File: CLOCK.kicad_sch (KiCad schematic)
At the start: 5 parts, among them X1 S3D50.000000B20F30T

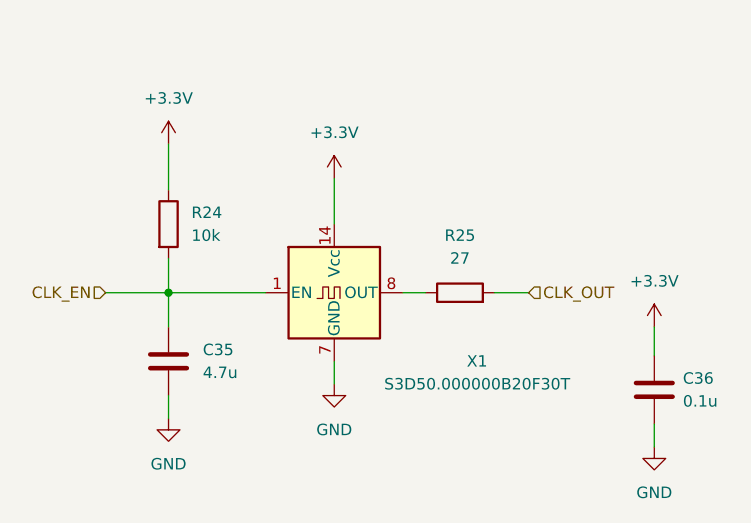
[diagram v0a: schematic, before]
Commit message: Add some more footprints
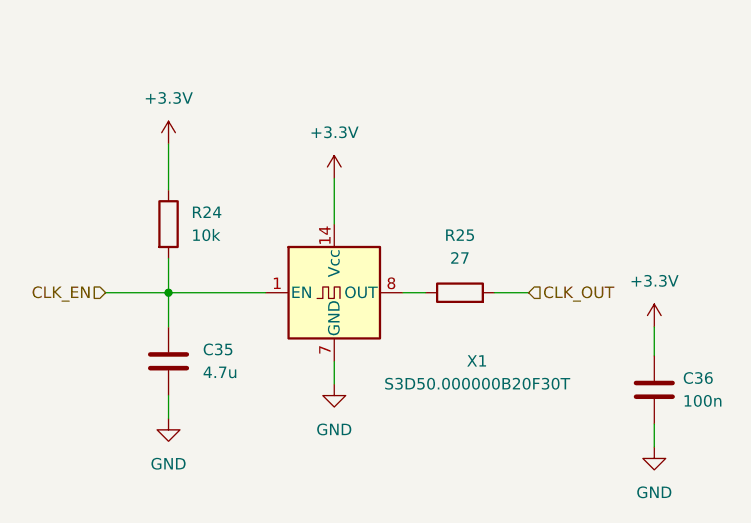
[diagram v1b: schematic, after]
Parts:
- C35: footprint (none) -> Capacitor_SMD:C_0603_1608Metric_Pad1.08x0.95mm_HandSolder
- C36: value 0.1u -> 100n; footprint (none) -> Capacitor_SMD:C_0603_1608Metric_Pad1.08x0.95mm_HandSolder
- R24, R25: footprint (none) -> Resistor_SMD:R_0603_1608Metric_Pad0.98x0.95mm_HandSolder
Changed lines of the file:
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@@
       (effects (font (size 1.27 1.27)) (justify left))
     )
-    (property "Value" "0.1u" (id 1) (at 191.77 108.5849 0)
+    (property "Value" "100n" (id 1) (at 191.77 108.5849 0)
       (effects (font (size 1.27 1.27)) (justify left))
     )
-    (property "Footprint" "" (id 2) (at 189.5602 111.125 0)
+    (property "Footprint" "Capacitor_SMD:C_0603_1608Metric_Pad1.08x0.95mm_HandSolder" (id 2) (at 189.5602 111.125 0)
       (effects (font (size 1.27 1.27)) hide)
     )
@@
       (effects (font (size 1.27 1.27)) (justify left))
     )
-    (property "Footprint" "" (id 2) (at 132.842 88.9 90)
+    (property "Footprint" "Resistor_SMD:R_0603_1608Metric_Pad0.98x0.95mm_HandSolder" (id 2) (at 132.842 88.9 90)
       (effects (font (size 1.27 1.27)) hide)
     )
@@
     (property "Reference" "R25" (id 0) (at 167.005 90.17 90))
     (property "Value" "27" (id 1) (at 167.005 92.71 90))
-    (property "Footprint" "" (id 2) (at 167.005 98.298 90)
+    (property "Footprint" "Resistor_SMD:R_0603_1608Metric_Pad0.98x0.95mm_HandSolder" (id 2) (at 167.005 98.298 90)
       (effects (font (size 1.27 1.27)) hide)
     )
@@
       (effects (font (size 1.27 1.27)) (justify left))
     )
-    (property "Footprint" "" (id 2) (at 135.5852 107.95 0)
+    (property "Footprint" "Capacitor_SMD:C_0603_1608Metric_Pad1.08x0.95mm_HandSolder" (id 2) (at 135.5852 107.95 0)
       (effects (font (size 1.27 1.27)) hide)
     )

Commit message: basic ETH layout
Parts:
- X1: footprint (none) -> project specific:XTAL_TSX-3225_16.0000MF18X-AC3
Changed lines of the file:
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@@
     (property "Reference" "X1" (id 0) (at 168.91 104.14 0))
     (property "Value" "S3D50.000000B20F30T" (id 1) (at 168.91 106.68 0))
-    (property "Footprint" "" (id 2) (at 164.465 105.41 0)
+    (property "Footprint" "project specific:XTAL_TSX-3225_16.0000MF18X-AC3" (id 2) (at 164.465 105.41 0)
       (effects (font (size 1.27 1.27)) hide)
     )

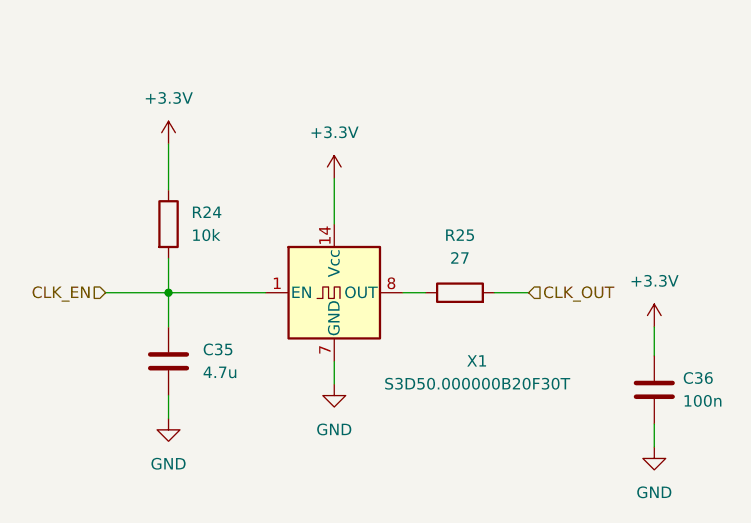
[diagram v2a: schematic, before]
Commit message: layout fixes
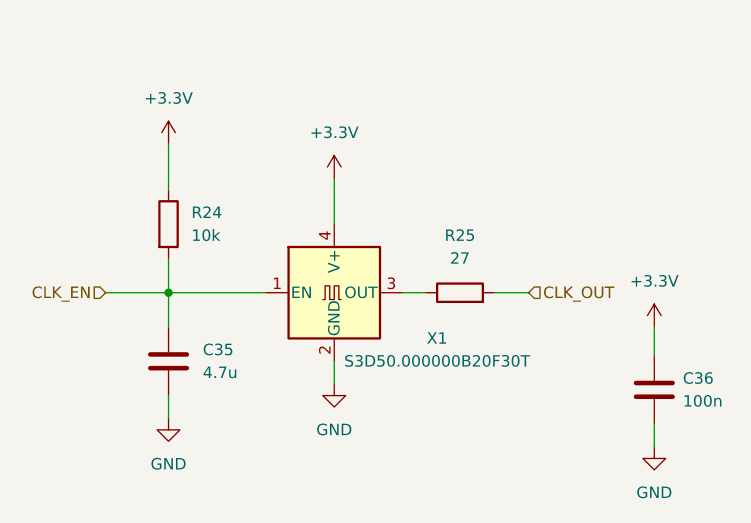
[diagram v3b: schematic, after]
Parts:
- removed X1: S3D50.000000B20F30T, project specific:XTAL_TSX-3225_16.0000MF18X-AC3, symbol Oscillator:CXO_DIP14
- added X1: S3D50.000000B20F30T, project specific:XTAL_TSX-3225_16.0000MF18X-AC3, symbol Oscillator:XO32
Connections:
- net +3.3V: now also X1.4 (V+)
- net CLK_EN: now also X1.1 (EN)
- net GND: now also X1.2 (GND)
- net at R25.1: now also X1.3 (OUT)
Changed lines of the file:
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@@
     (pin "1")
   )
-  (symbol (lib_id "Oscillator:CXO_DIP14") (at 153.035 96.52 0) (unit 1)
+  (symbol (lib_id "Oscillator:XO32") (at 153.035 96.52 0) (unit 1)
     (in_bom yes) (on_board yes)
-    (property "Reference" "X1" (id 0) (at 168.91 104.14 0))
-    (property "Value" "S3D50.000000B20F30T" (id 1) (at 168.91 106.68 0))
-    (property "Footprint" "project specific:XTAL_TSX-3225_16.0000MF18X-AC3" (id 2) (at 164.465 105.41 0)
+    (property "Reference" "X1" (id 0) (at 164.465 101.6 0))
+    (property "Value" "S3D50.000000B20F30T" (id 1) (at 164.465 104.14 0))
+    (property "Footprint" "project specific:XTAL_TSX-3225_16.0000MF18X-AC3" (id 2) (at 170.815 105.41 0)
       (effects (font (size 1.27 1.27)) hide)
     )
@@
     )
     (pin "1")
-    (pin "14")
-    (pin "7")
-    (pin "8")
+    (pin "2")
+    (pin "3")
+    (pin "4")
   )
   (symbol (lib_id "Device:R") (at 167.005 96.52 90) (unit 1)

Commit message: Add more LCSC markings, change to electrolytic caps :
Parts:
- C35: LCSC (none) -> C8032
- C36: LCSC (none) -> C282519
- R24: LCSC (none) -> C2930027
- R25: LCSC (none) -> C5140675
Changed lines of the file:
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@@
+      (effects (font (size 1.27 1.27)) hide)
+    )
+    (property "LCSC" "C282519" (id 4) (at 188.595 107.315 0)
       (effects (font (size 1.27 1.27)) hide)
     )
@@
       (effects (font (size 1.27 1.27)) hide)
     )
+    (property "LCSC" "C2930027" (id 4) (at 134.62 88.9 0)
+      (effects (font (size 1.27 1.27)) hide)
+    )
     (pin "1")
     (pin "2")
@@
     )
     (property "Datasheet" "~" (id 3) (at 167.005 96.52 0)
+      (effects (font (size 1.27 1.27)) hide)
+    )
+    (property "LCSC" "C5140675" (id 4) (at 167.005 96.52 90)
       (effects (font (size 1.27 1.27)) hide)
     )
@@
       (effects (font (size 1.27 1.27)) hide)
     )
+    (property "LCSC" "C8032" (id 4) (at 134.62 104.14 0)
+      (effects (font (size 1.27 1.27)) hide)
+    )

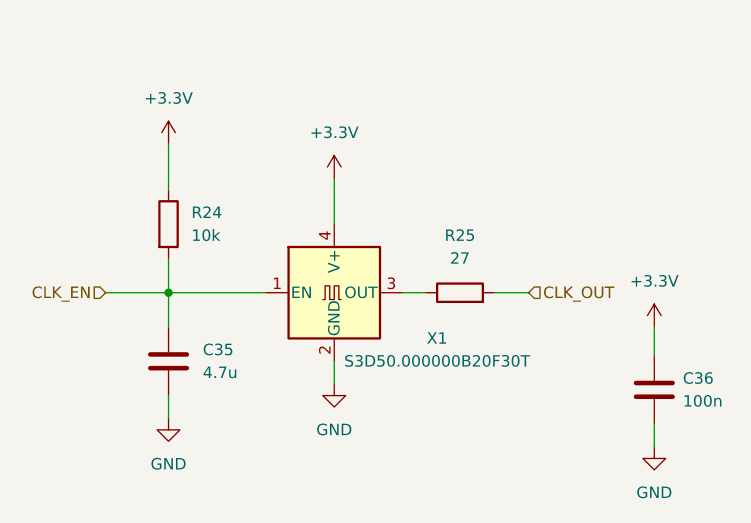
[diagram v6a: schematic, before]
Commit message: Update schematic for V1.1
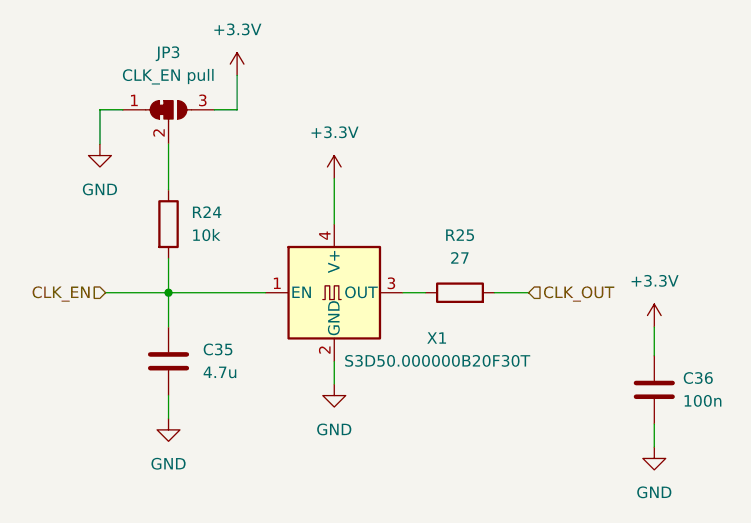
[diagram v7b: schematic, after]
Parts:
- added JP3: CLK_EN pull, Jumper:SolderJumper-3_P1.3mm_Bridged12_RoundedPad1.0x1.5mm, symbol Jumper:SolderJumper_3_Bridged12
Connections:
- net +3.3V: now also JP3.3 (B); no longer R24.1
- net GND: now also JP3.1 (A)
- new net: JP3.2 (C), R24.1
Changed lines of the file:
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@@
+	(wire
+		(pts
+			(xy 127 76.2) (xy 127 80.01)
+		)
+		(stroke
+			(width 0)
+			(type default)
+		)
+	)
 	(wire
 		(pts
@@
 	(wire
 		(pts
+			(xy 142.24 76.2) (xy 142.24 72.39)
+		)
+		(stroke
+			(width 0)
+			(type default)
+		)
+	)
+	(wire
+		(pts
 			(xy 134.62 96.52) (xy 134.62 92.71)
 		)
@@
 		(pts
 			(xy 188.595 111.125) (xy 188.595 113.665)
+		)
+		(stroke
+			(width 0)
+			(type default)
+		)
+	)
+	(wire
+		(pts
+			(xy 139.7 76.2) (xy 142.24 76.2)
+		)
+		(stroke
+			(width 0)
+			(type default)
+		)
+	)
+	(wire
+		(pts
+			(xy 127 76.2) (xy 129.54 76.2)
 		)
 		(stroke
@@
 	(symbol
 		(lib_id "power:GND")
+		(at 127 80.01 0)
+		(unit 1)
+		(exclude_from_sim no)
+		(in_bom yes)
+		(on_board yes)
+		(dnp no)
+		(fields_autoplaced yes)
+		(property "Reference" "#PWR08"
+			(at 127 86.36 0)
+			(effects
+				(font
+					(size 1.27 1.27)
+				)
+				(hide yes)
+			)
+		)
+		(property "Value" "GND"
+			(at 127 85.09 0)
+			(effects
+				(font
+					(size 1.27 1.27)
+				)
+			)
+		)
+		(property "Footprint" ""
+			(at 127 80.01 0)
+			(effects
+				(font
+					(size 1.27 1.27)
+				)
+				(hide yes)
+			)
+		)
+		(property "Datasheet" ""
+			(at 127 80.01 0)
+			(effects
+				(font
+					(size 1.27 1.27)
+				)
+				(hide yes)
+			)
+		)
+		(property "Description" ""
+			(at 127 80.01 0)
+			(effects
+				(font
+					(size 1.27 1.27)
+				)
+				(hide yes)
+			)
+		)
+		(pin "1"
+		)
+		(instances
+			(project "Zamkonator"
+				(path "/727d6c0a-a0ef-4feb-9656-3db3cb90564a/2418ed7a-6668-472e-9550-09c70e5c9c72"
+					(reference "#PWR08")
+					(unit 1)
+				)
+			)
+		)
+	)
+	(symbol
+		(lib_id "power:GND")
 		(at 134.62 110.49 0)
 		(unit 1)
@@
 	(symbol
 		(lib_id "power:+3.3V")
-		(at 134.62 80.01 0)
+		(at 142.24 72.39 0)
 		(unit 1)
 		(exclude_from_sim no)
@@
 		(fields_autoplaced yes)
 		(property "Reference" "#PWR049"
-			(at 134.62 83.82 0)
+			(at 142.24 76.2 0)
 			(effects
 				(font
@@
 		)
 		(property "Value" "+3.3V"
-			(at 134.62 74.93 0)
+			(at 142.24 67.31 0)
 			(effects
 				(font
@@
 		)
 		(property "Footprint" ""
-			(at 134.62 80.01 0)
+			(at 142.24 72.39 0)
 			(effects
 				(font
@@
 		)
 		(property "Datasheet" ""
-			(at 134.62 80.01 0)
+			(at 142.24 72.39 0)
 			(effects
 				(font
@@
 		)
 		(property "Description" ""
-			(at 134.62 80.01 0)
+			(at 142.24 72.39 0)
 			(effects
 				(font
@@
 				(path "/727d6c0a-a0ef-4feb-9656-3db3cb90564a/2418ed7a-6668-472e-9550-09c70e5c9c72"
 					(reference "#PWR049")
+					(unit 1)
+				)
+			)
+		)
+	)
+	(symbol
+		(lib_id "Jumper:SolderJumper_3_Bridged12")
+		(at 134.62 76.2 0)
+		(unit 1)
+		(exclude_from_sim yes)
+		(in_bom no)
+		(on_board yes)
+		(dnp no)
+		(fields_autoplaced yes)
+		(property "Reference" "JP3"
+			(at 134.62 69.85 0)
+			(effects
+				(font
+					(size 1.27 1.27)
+				)
+			)
+		)
+		(property "Value" "CLK_EN pull"
+			(at 134.62 72.39 0)
+			(effects
+				(font
+					(size 1.27 1.27)
+				)
+			)
+		)
+		(property "Footprint" "Jumper:SolderJumper-3_P1.3mm_Bridged12_RoundedPad1.0x1.5mm"
+			(at 134.62 76.2 0)
+			(effects
+				(font
+					(size 1.27 1.27)
+				)
+				(hide yes)
+			)
+		)
+		(property "Datasheet" "~"
+			(at 134.62 76.2 0)
+			(effects
+				(font
+					(size 1.27 1.27)
+				)
+				(hide yes)
+			)
+		)
+		(property "Description" "3-pole Solder Jumper, pins 1+2 closed/bridged"
+			(at 134.62 76.2 0)
+			(effects
+				(font
+					(size 1.27 1.27)
+				)
+				(hide yes)
+			)
+		)
+		(pin "1"
+		)
+		(pin "2"
+		)
+		(pin "3"
+		)
+		(instances
+			(project ""
+				(path "/727d6c0a-a0ef-4feb-9656-3db3cb90564a/2418ed7a-6668-472e-9550-09c70e5c9c72"
+					(reference "JP3")
 					(unit 1)
 				)
@@
 			)
 		)
-		(property "Datasheet" ""
+		(property "Datasheet" "https://www.lcsc.com/datasheet/lcsc_datasheet_2209071730_Shenzhen-SCTF-Elec-S3D50-000000B20F30T_C387445.pdf"
 			(at 150.495 96.52 0)
 			(effects

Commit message: BOM updates & schematic fixes
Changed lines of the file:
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@@
 (kicad_sch
-	(version 20231120)
+	(version 20250114)
 	(generator "eeschema")
-	(generator_version "8.0")
+	(generator_version "9.0")
 	(paper "A4")
 	(junction
@@
 		(shape input)
 		(at 174.625 96.52 0)
-		(fields_autoplaced yes)
 		(effects
 			(font
@@
 		(shape input)
 		(at 127.635 96.52 180)
-		(fields_autoplaced yes)
 		(effects
 			(font
